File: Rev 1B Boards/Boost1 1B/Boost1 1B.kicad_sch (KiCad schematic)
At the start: 3 parts, among them J18 Banana 2P, J19 Banana 2P, J20 Banana 2P

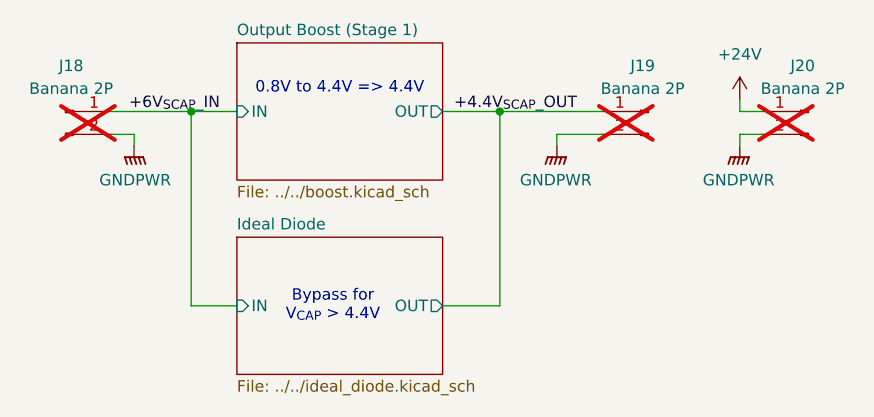
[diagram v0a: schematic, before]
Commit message: Completed Boost stage 1 layout
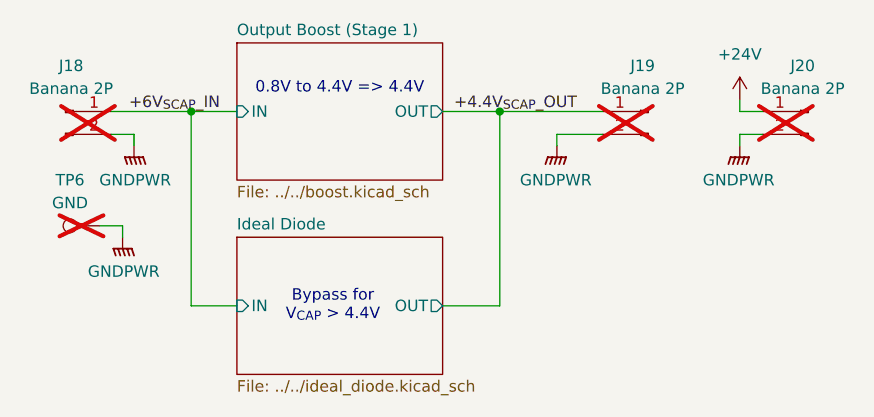
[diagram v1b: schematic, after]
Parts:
- added TP6: GND, TestPoint:TestPoint_Bridge_Pitch2.0mm_Drill0.7mm, symbol Connector:TestPoint
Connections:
- net GNDPWR: now also TP6.1
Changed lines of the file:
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@@
+	(wire
+		(pts
+			(xy 59.69 72.39) (xy 62.23 72.39)
+		)
+		(stroke
+			(width 0)
+			(type default)
+		)
+	)
 	(wire
 		(pts
@@
 		(pts
 			(xy 104.14 59.69) (xy 104.14 81.28)
+		)
+		(stroke
+			(width 0)
+			(type default)
+		)
+	)
+	(wire
+		(pts
+			(xy 62.23 72.39) (xy 62.23 73.66)
 		)
 		(stroke
@@
 			)
 			(justify right bottom)
+		)
+	)
+	(symbol
+		(lib_id "Connector:TestPoint")
+		(at 59.69 72.39 90)
+		(unit 1)
+		(exclude_from_sim no)
+		(in_bom yes)
+		(on_board yes)
+		(dnp yes)
+		(property "Reference" "TP6"
+			(at 56.388 67.31 90)
+			(effects
+				(font
+					(size 1.27 1.27)
+				)
+			)
+		)
+		(property "Value" "GND"
+			(at 56.388 69.85 90)
+			(effects
+				(font
+					(size 1.27 1.27)
+				)
+			)
+		)
+		(property "Footprint" "TestPoint:TestPoint_Bridge_Pitch2.0mm_Drill0.7mm"
+			(at 59.69 67.31 0)
+			(effects
+				(font
+					(size 1.27 1.27)
+				)
+				(hide yes)
+			)
+		)
+		(property "Datasheet" "~"
+			(at 59.69 67.31 0)
+			(effects
+				(font
+					(size 1.27 1.27)
+				)
+				(hide yes)
+			)
+		)
+		(property "Description" "test point"
+			(at 59.69 72.39 0)
+			(effects
+				(font
+					(size 1.27 1.27)
+				)
+				(hide yes)
+			)
+		)
+		(property "Sim.Device" ""
+			(at 59.69 72.39 0)
+			(effects
+				(font
+					(size 1.27 1.27)
+				)
+			)
+		)
+		(property "Sim.Pins" ""
+			(at 59.69 72.39 0)
+			(effects
+				(font
+					(size 1.27 1.27)
+				)
+			)
+		)
+		(property "Sim.Type" ""
+			(at 59.69 72.39 0)
+			(effects
+				(font
+					(size 1.27 1.27)
+				)
+			)
+		)
+		(property "Height" ""
+			(at 59.69 72.39 0)
+			(effects
+				(font
+					(size 1.27 1.27)
+				)
+			)
+		)
+		(property "Manufacturer_Name" ""
+			(at 59.69 72.39 0)
+			(effects
+				(font
+					(size 1.27 1.27)
+				)
+			)
+		)
+		(property "Manufacturer_Part_Number" ""
+			(at 59.69 72.39 0)
+			(effects
+				(font
+					(size 1.27 1.27)
+				)
+			)
+		)
+		(property "Mouser Price/Stock" ""
+			(at 59.69 72.39 0)
+			(effects
+				(font
+					(size 1.27 1.27)
+				)
+			)
+		)
+		(pin "1"
+		)
+		(instances
+			(project "Boost1 1B"
+				(path "/80afba09-f71a-481c-a343-2cbd993e7569"
+					(reference "TP6")
+					(unit 1)
+				)
+			)
 		)
 	)
@@
 					(unit 1)
 				)
+			)
+		)
+	)
+	(symbol
+		(lib_id "power:GNDPWR")
+		(at 62.23 73.66 0)
+		(mirror y)
+		(unit 1)
+		(exclude_from_sim no)
+		(in_bom yes)
+		(on_board yes)
+		(dnp no)
+		(fields_autoplaced yes)
+		(property "Reference" "#PWR027"
+			(at 62.23 78.74 0)
+			(effects
+				(font
+					(size 1.27 1.27)
+				)
+				(hide yes)
+			)
+		)
+		(property "Value" "GNDPWR"
+			(at 62.357 77.47 0)
+			(effects
+				(font
+					(size 1.27 1.27)
+				)
+			)
+		)
+		(property "Footprint" ""
+			(at 62.23 74.93 0)
+			(effects
+				(font
+					(size 1.27 1.27)
+				)
+				(hide yes)
+			)
+		)
+		(property "Datasheet" ""
+			(at 62.23 74.93 0)
+			(effects
+				(font
+					(size 1.27 1.27)
+				)
+				(hide yes)
+			)
+		)
+		(property "Description" "Power symbol creates a global label with name \"GNDPWR\" , global ground"
+			(at 62.23 73.66 0)
+			(effects
+				(font
+					(size 1.27 1.27)
+				)
+				(hide yes)
+			)
+		)
+		(pin "1"
+		)
+		(instances
+			(project "Boost1 1B"
+				(path "/80afba09-f71a-481c-a343-2cbd993e7569"
+					(reference "#PWR027")
+					(unit 1)
+				)

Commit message: Replace most banana jacks with XT connectors
+ update library
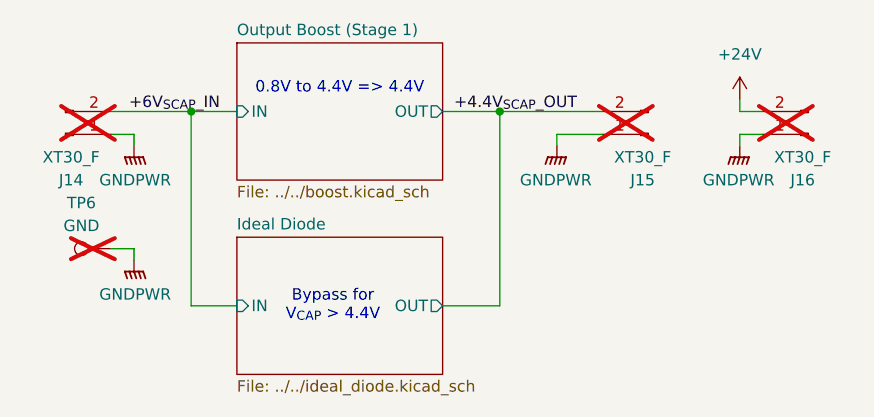
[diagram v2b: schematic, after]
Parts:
- removed J18, J19, J20: Banana 2P, Connector:Banana_Jack_2Pin, symbol Connector:Conn_01x02_Pin
- added J14, J15, J16: XT30_F, Connector_AMASS:AMASS_XT30U-F_1x02_P5.0mm_Vertical, symbol Connector:Conn_01x02_Pin
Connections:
- net +24V: now also J16.2 (Pin_2)
- net +4.4V_{SCAP}_OUT: now also J15.2 (Pin_2)
- net +6V_{SCAP}_IN: now also J14.2 (Pin_2)
- net GNDPWR: now also J14.1 (Pin_1), J15.1 (Pin_1), J16.1 (Pin_1)
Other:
- moved on the sheet: TP6
